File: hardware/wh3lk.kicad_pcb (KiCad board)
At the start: 4 copper layers, 41.5 x 33.5 mm, 23 parts, among them J1 Eurorack_Power, J2 Conn_01x08_Pin, U1 LD1117S33TR_SOT223, U2 LM4040DBZ-10

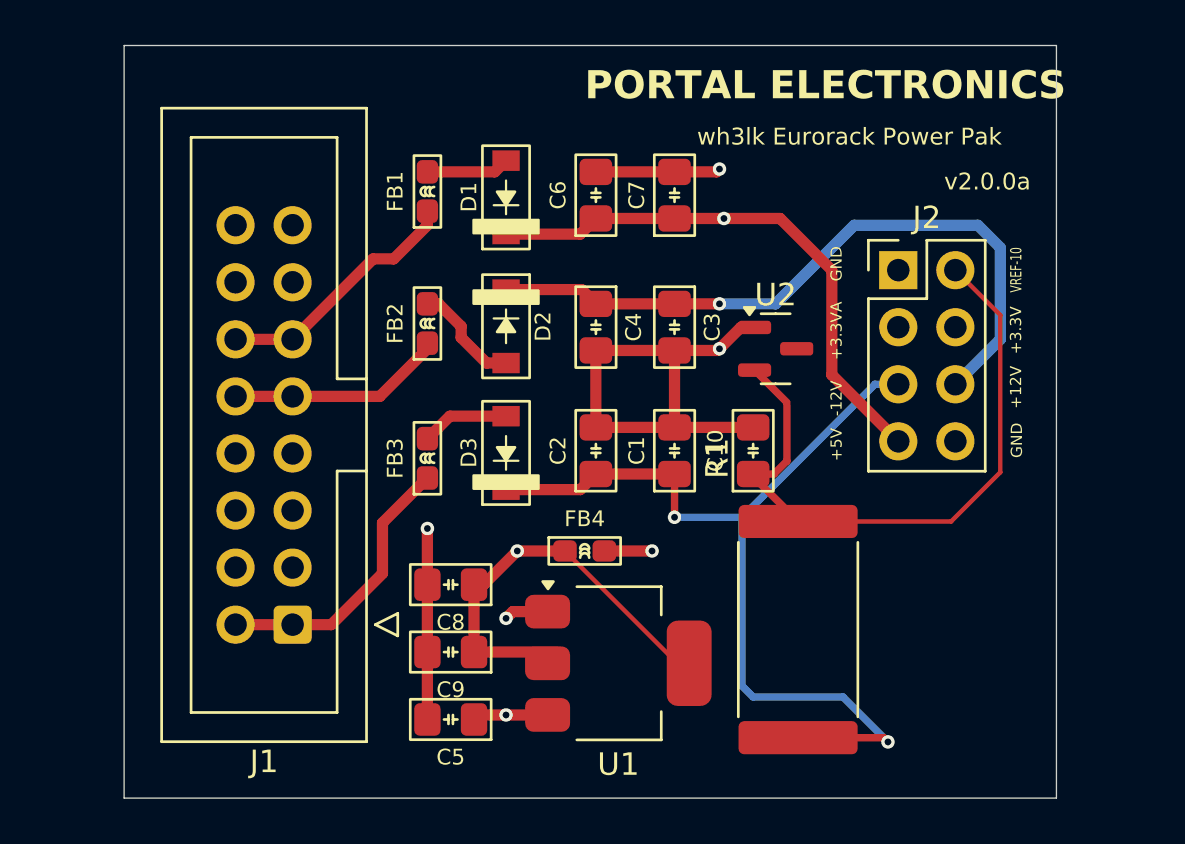
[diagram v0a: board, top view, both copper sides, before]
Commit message: Corrected resistor package, deleted unused files and gerbers
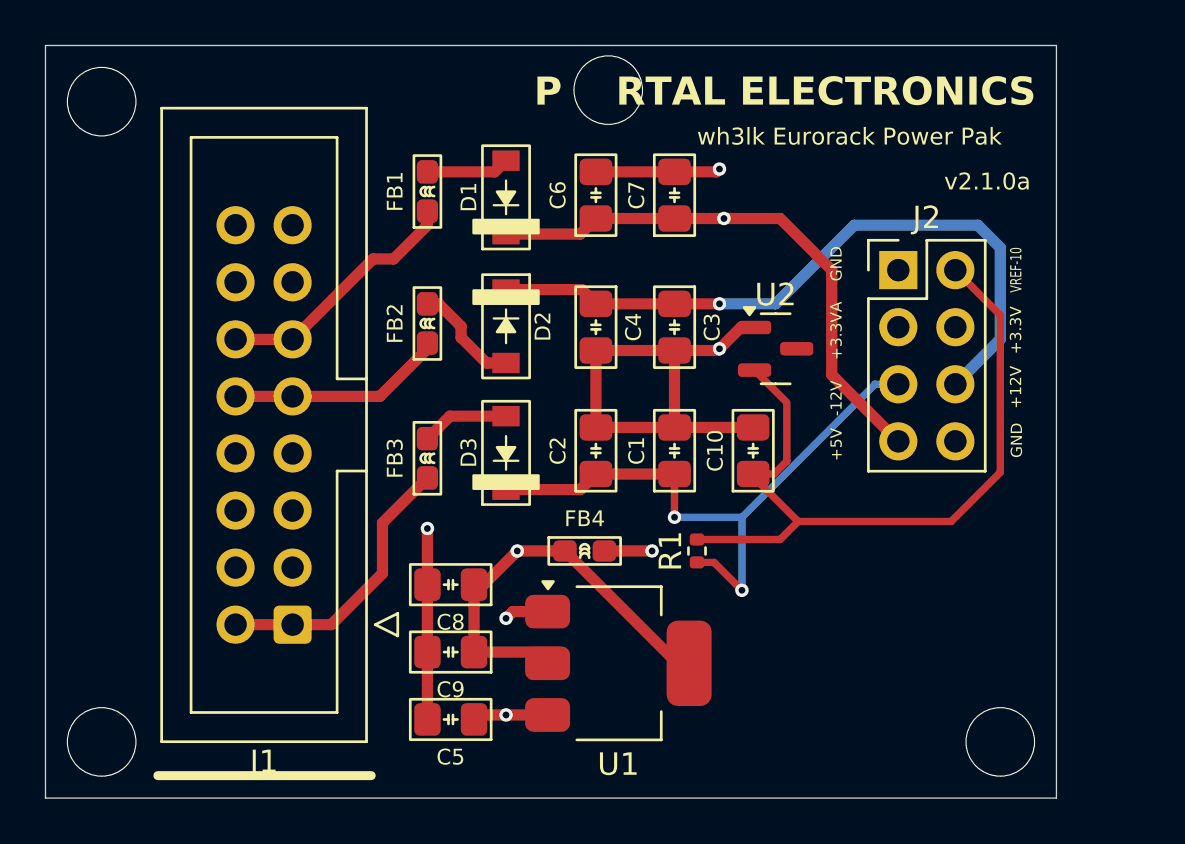
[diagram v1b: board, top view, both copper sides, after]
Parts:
- R1: footprint Resistor_SMD:R_4020_10251Metric -> Resistor_SMD:R_0402_1005Metric
- moved R1 5.70 mm to (82.0, 81.0)
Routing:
- net -12V: track 41.2 -> 27.9 mm
- net VREF-10: track 29.1 -> 33.9 mm
- net (no net): vias 0 -> 4
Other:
- board size 41.5 x 33.5 mm -> 45 x 33.5 mm
- board text added: "P RTAL ELECTRONICS"
- board text removed: "${COMPANY}"

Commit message: Moved mounting holes to GND
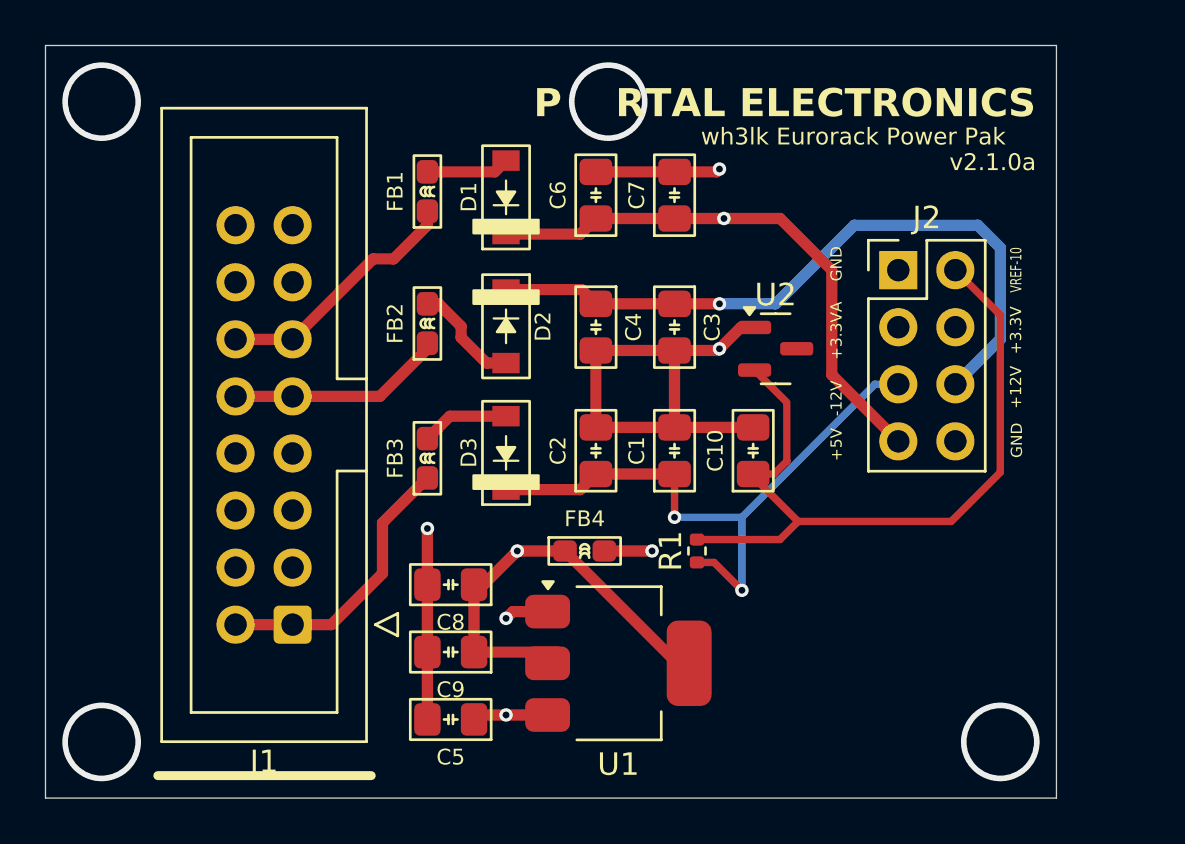
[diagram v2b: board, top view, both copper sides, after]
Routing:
- net GND: track 143.4 -> 296.0 mm, vias 4 -> 8
- net (no net): vias 4 -> 0
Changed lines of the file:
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@@
 	)
 	(gr_text "${REVISION}"
-		(at 93 65 0)
+		(at 93.237266 64.137403 0)
 		(layer "F.SilkS")
 		(effects
@@
 	)
 	(gr_text "P    RTAL ELECTRONICS"
-		(at 74.740704 61.285196 0)
+		(at 74.726442 61.798593 0)
 		(layer "F.SilkS")
 		(effects
@@
 	)
 	(gr_text "wh3lk Eurorack Power Pak"
-		(at 82 63 0)
+		(at 82.170703 62.99652 0)
 		(layer "F.SilkS")
 		(effects
@@
 		)
 	)
-	(via
-		(at 78.049264 60.486578)
-		(size 3.1)
-		(drill 3)
-		(layers "F.Cu" "B.Cu")
-		(net 0)
-	)
-	(via
-		(at 55.5 61)
-		(size 3.1)
-		(drill 3)
-		(layers "F.Cu" "B.Cu")
-		(net 0)
-	)
-	(via
-		(at 55.5 89.5)
-		(size 3.1)
-		(drill 3)
-		(layers "F.Cu" "B.Cu")
-		(net 0)
-	)
-	(via
-		(at 95.5 89.5)
-		(size 3.1)
-		(drill 3)
-		(layers "F.Cu" "B.Cu")
-		(net 0)
-	)
 	(segment
 		(start 83.95 71.05)
@@
 		(width 0.5)
 		(layer "F.Cu")
+		(net 1)
+	)
+	(via
+		(at 78.049264 61)
+		(size 3.5)
+		(drill 3)
+		(layers "F.Cu" "B.Cu")
+		(free yes)
+		(net 1)
+	)
+	(via
+		(at 55.5 61)
+		(size 3.5)
+		(drill 3)
+		(layers "F.Cu" "B.Cu")
+		(free yes)
+		(net 1)
+	)
+	(via
+		(at 55.5 89.5)
+		(size 3.5)
+		(drill 3)
+		(layers "F.Cu" "B.Cu")
+		(free yes)
 		(net 1)
 	)
@@
 		(net 1)
 	)
+	(via
+		(at 95.5 89.5)
+		(size 3.5)
+		(drill 3)
+		(layers "F.Cu" "B.Cu")
+		(free yes)
+		(net 1)
+	)
+	(segment
+		(start 56.84 76.66)
+		(end 55.5 78)
+		(width 0.5)
+		(layer "In1.Cu")
+		(net 1)
+	)
 	(segment
 		(start 73.5 84)
@@
 	)
 	(segment
+		(start 55.5 89.5)
+		(end 95.5 89.5)
+		(width 0.5)
+		(layer "In1.Cu")
+		(net 1)
+	)
+	(segment
+		(start 95.5 76.5)
+		(end 95.5 61)
+		(width 0.5)
+		(layer "In1.Cu")
+		(net 1)
+	)
+	(segment
+		(start 95.5 76.5)
+		(end 95.12 76.12)
+		(width 0.5)
+		(layer "In1.Cu")
+		(net 1)
+	)
+	(segment
+		(start 91 61)
+		(end 78.049264 61)
+		(width 0.5)
+		(layer "In1.Cu")
+		(net 1)
+	)
+	(segment
 		(start 83 72)
 		(end 68.66 72)
@@
 	)
 	(segment
+		(start 61.46 76.66)
+		(end 57.16 76.66)
+		(width 0.5)
+		(layer "In1.Cu")
+		(net 1)
+	)
+	(segment
+		(start 90.96 68.5)
+		(end 90.96 61.04)
+		(width 0.5)
+		(layer "In1.Cu")
+		(net 1)
+	)
+	(segment
 		(start 85.62 84)
 		(end 93.5 76.12)
@@
 	)
 	(segment
+		(start 57.16 76.66)
+		(end 55.5 75)
+		(width 0.5)
+		(layer "In1.Cu")
+		(net 1)
+	)
+	(segment
 		(start 61.46 76.66)
 		(end 64 76.66)
@@
 	)
 	(segment
+		(start 55.5 61)
+		(end 78.049264 61)
+		(width 0.5)
+		(layer "In1.Cu")
+		(net 1)
+	)
+	(segment
 		(start 64 76.66)
 		(end 64 79.2)
@@
 	)
 	(segment
+		(start 55.5 78)
+		(end 55.5 89.5)
+		(width 0.5)
+		(layer "In1.Cu")
+		(net 1)
+	)
+	(segment
 		(start 85 66)
 		(end 85 70.96)
@@
 	)
 	(segment
+		(start 55.5 75)
+		(end 55.5 61)
+		(width 0.5)
+		(layer "In1.Cu")
+		(net 1)
+	)
+	(segment
 		(start 65.74 80)
 		(end 70 80)
@@
 	)
 	(segment
+		(start 95.5 89.5)
+		(end 95.5 76.5)
+		(width 0.5)
+		(layer "In1.Cu")
+		(net 1)
+	)
+	(segment
 		(start 83 64)
 		(end 85 66)
@@
 	)
 	(segment
+		(start 57.16 76.66)
+		(end 56.84 76.66)
+		(width 0.5)
+		(layer "In1.Cu")
+		(net 1)
+	)
+	(segment
 		(start 72.76 84.74)
 		(end 67 84.74)
@@
 	)
 	(segment
+		(start 95.5 61)
+		(end 91 61)
+		(width 0.5)
+		(layer "In1.Cu")
+		(net 1)
+	)
+	(segment
 		(start 64 81.74)
 		(end 61.46 79.2)
@@
 	)
 	(segment
+		(start 90.96 61.04)
+		(end 91 61)
+		(width 0.5)
+		(layer "In1.Cu")
+		(net 1)
+	)
+	(segment
 		(start 87.46 68.5)
 		(end 90.96 68.5)
 		(width 0.5)
 		(layer "In1.Cu")
+		(net 1)
+	)
+	(segment
+		(start 95.12 76.12)
+		(end 93.5 76.12)
+		(width 0.5)
+		(layer "In1.Cu")

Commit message: bom generation
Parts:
- C9: value 22uF -> 100nF
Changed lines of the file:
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@@
 			)
 		)
-		(property "LCSC" ""
+		(property "LCSC" "C45783"
 			(at 0 0 90)
 			(unlocked yes)
@@
 			)
 		)
+		(property "LCSC" "C552852"
+			(at 0 0 90)
+			(unlocked yes)
+			(layer "F.Fab")
+			(hide yes)
+			(effects
+				(font
+					(size 1 1)
+					(thickness 0.15)
+				)
+			)
+		)
 		(property ki_fp_filters "TO-???* *_Diode_* *SingleDiode* D_*")
 		(sheetname "Power Prep")
@@
 			)
 		)
+		(property "LCSC" "C45783"
+			(at 0 0 90)
+			(unlocked yes)
+			(layer "F.Fab")
+			(hide yes)
+			(effects
+				(font
+					(size 1 1)
+					(thickness 0.15)
+				)
+			)
+		)
 		(property ki_fp_filters "C_*")
 		(sheetname "Power Prep")
@@
 			)
 		)
+		(property "LCSC" "C45783"
+			(at 0 0 -90)
+			(unlocked yes)
+			(layer "F.Fab")
+			(hide yes)
+			(effects
+				(font
+					(size 1 1)
+					(thickness 0.15)
+				)
+			)
+		)
 		(property ki_fp_filters "C_*")
 		(sheetname "Power Prep")
@@
 			)
 		)
-		(property "Value" "22uF"
+		(property "Value" "100nF"
 			(at 0 1.68 180)
 			(layer "F.Fab")
@@
 			)
 		)
+		(property "LCSC" "C7411876"
+			(at 0 0 180)
+			(unlocked yes)
+			(layer "F.Fab")
+			(hide yes)
+			(effects
+				(font
+					(size 1 1)
+					(thickness 0.15)
+				)
+			)
+		)
 		(property ki_fp_filters "C_*")
 		(sheetname "Power Prep")
@@
 			)
 		)
+		(property "LCSC" "C552852"
+			(at 0 0 90)
+			(unlocked yes)
+			(layer "F.Fab")
+			(hide yes)
+			(effects
+				(font
+					(size 1 1)
+					(thickness 0.15)
+				)
+			)
+		)
 		(property ki_fp_filters "TO-???* *_Diode_* *SingleDiode* D_*")
 		(sheetname "Power Prep")
@@
 			)
 		)
+		(property "LCSC" "C45783"
+			(at 0 0 90)
+			(unlocked yes)
+			(layer "F.Fab")
+			(hide yes)
+			(effects
+				(font
+					(size 1 1)
+					(thickness 0.15)
+				)
+			)
+		)
 		(property ki_fp_filters "C_*")
 		(sheetname "Power Prep")
@@
 			)
 		)
+		(property "LCSC" "C552852"
+			(at 0 0 -90)
+			(unlocked yes)
+			(layer "F.Fab")
+			(hide yes)
+			(effects
+				(font
+					(size 1 1)
+					(thickness 0.15)
+				)
+			)
+		)
 		(property ki_fp_filters "TO-???* *_Diode_* *SingleDiode* D_*")
 		(sheetname "Power Prep")
@@
 			)
 		)
+		(property "LCSC" "C7411876"
+			(at 0 0 180)
+			(unlocked yes)
+			(layer "F.Fab")
+			(hide yes)
+			(effects
+				(font
+					(size 1 1)
+					(thickness 0.15)
+				)
+			)
+		)
 		(property ki_fp_filters "C_*")
 		(sheetname "Power Prep")
@@
 			)
 		)
+		(property "LCSC" "C6549338"
+			(at 0 0 90)
+			(unlocked yes)
+			(layer "F.Fab")
+			(hide yes)
+			(effects
+				(font
+					(size 1 1)
+					(thickness 0.15)
+				)
+			)
+		)
 		(property ki_fp_filters "R_*")
 		(sheetname "Power Prep")
@@
 			)
 		)
+		(property "LCSC" "C45783"
+			(at 0 0 90)
+			(unlocked yes)
+			(layer "F.Fab")
+			(hide yes)
+			(effects
+				(font
+					(size 1 1)
+					(thickness 0.15)
+				)
+			)
+		)
 		(property ki_fp_filters "C_*")
 		(sheetname "Power Prep")
@@
 			)
 		)
+		(property "LCSC" "C45783"
+			(at 0 0 -90)
+			(unlocked yes)
+			(layer "F.Fab")
+			(hide yes)
+			(effects
+				(font
+					(size 1 1)
+					(thickness 0.15)
+				)
+			)
+		)
 		(property ki_fp_filters "C_*")
 		(sheetname "Power Prep")
@@
 			)
 		)
+		(property "LCSC" "C45783"
+			(at 0 0 180)
+			(unlocked yes)
+			(layer "F.Fab")
+			(hide yes)
+			(effects
+				(font
+					(size 1 1)
+					(thickness 0.15)
+				)
+			)
+		)
 		(property ki_fp_filters "C_*")
 		(sheetname "Power Prep")
@@
 				)
 			)
+		)
+		(property "LCSC" "C45783"
+			(at 0 0 90)
+			(unlocked yes)
+			(layer "F.Fab")
+			(hide yes)
+			(effects
+				(font
+					(size 1 1)
+					(thickness 0.15)
+				)
+			)

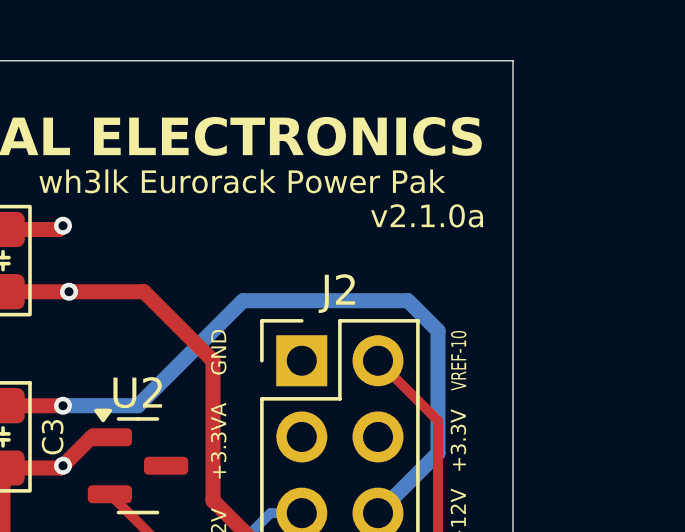
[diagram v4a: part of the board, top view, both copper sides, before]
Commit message: Removed ohm symbol to not break JCLPCB BOM
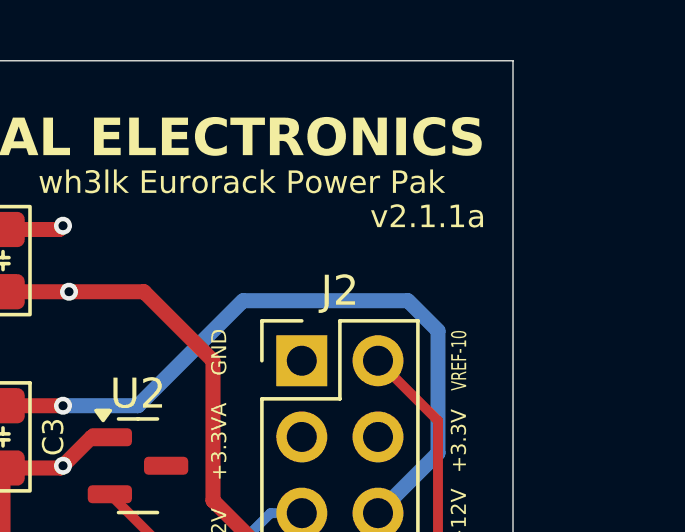
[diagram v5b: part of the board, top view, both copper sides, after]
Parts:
- R1: value 2k2Ω -> 2k2R
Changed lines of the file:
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@@
 		(title "wh3lk Eurorack Power Pak")
 		(date "2024-09-09")
-		(rev "v2.1.0a")
+		(rev "v2.1.1a")
 		(company "PORTAL ELECTRONICS")
 	)
@@
 			)
 		)
-		(property "Value" "2k2Ω"
+		(property "Value" "2k2R"
 			(at 0 1.17 90)
 			(layer "F.Fab")
